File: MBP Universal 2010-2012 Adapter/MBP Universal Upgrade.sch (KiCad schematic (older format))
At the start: 3 parts, among them J1 501745-0301, J3401 500913-0302, P1 AdapterPCIEContacts

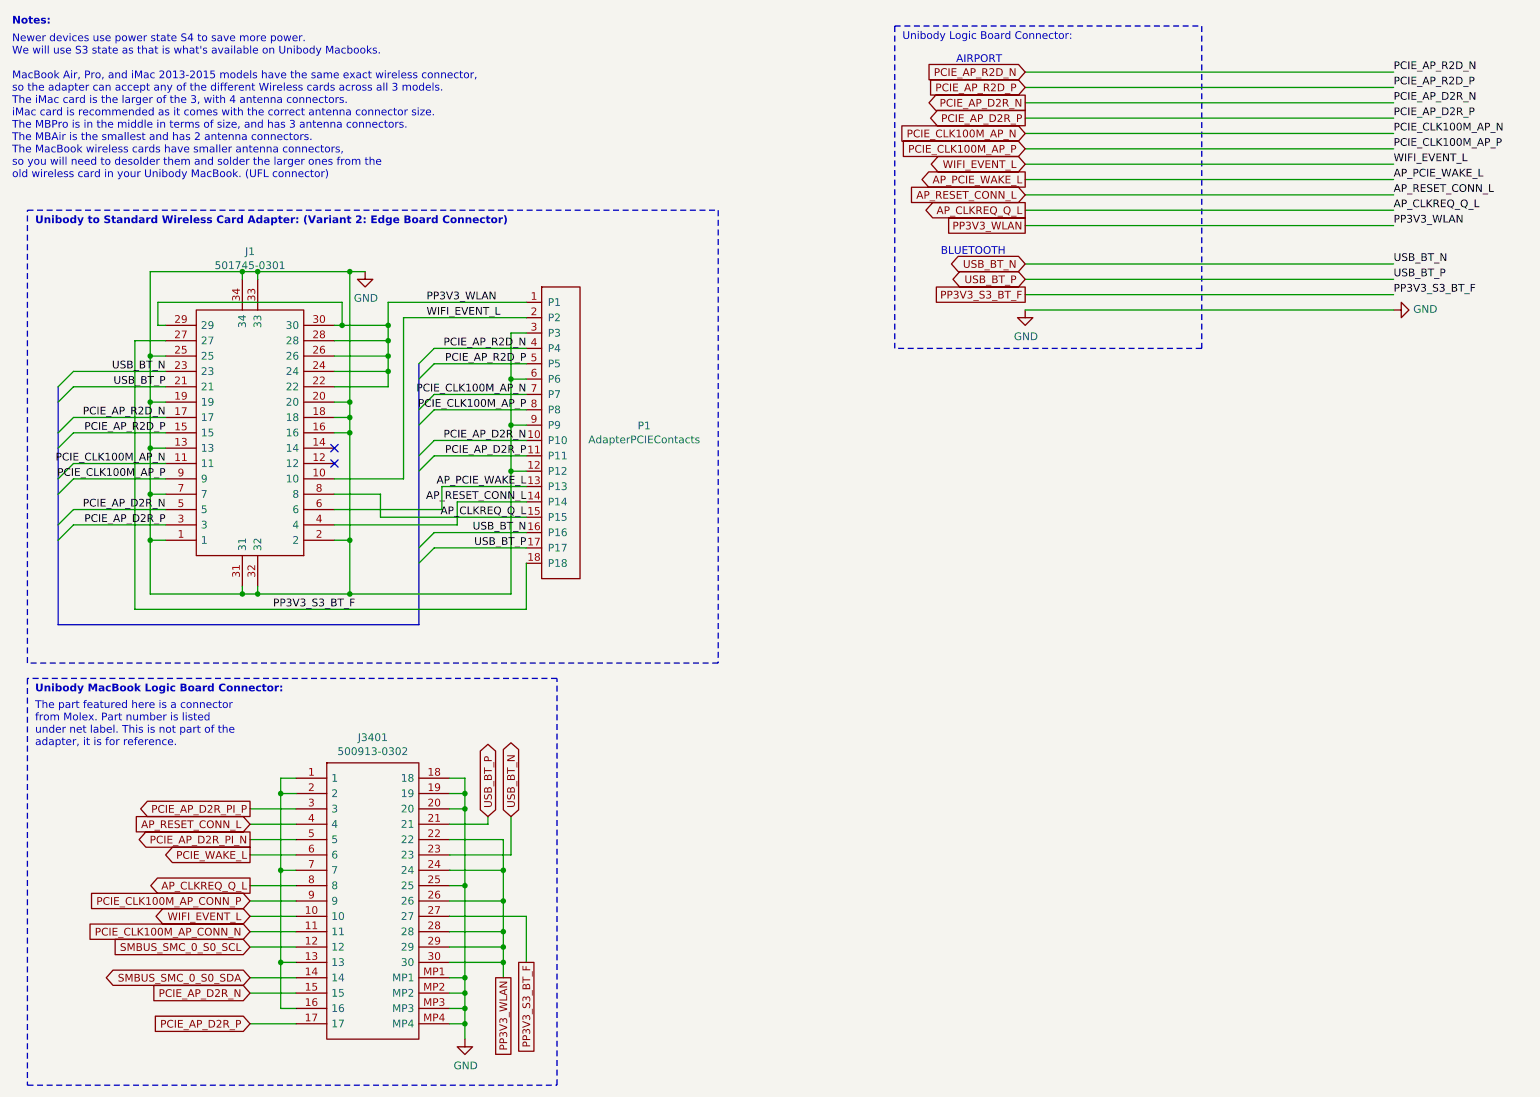
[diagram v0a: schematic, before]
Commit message: Release prototype for Universal part ready.
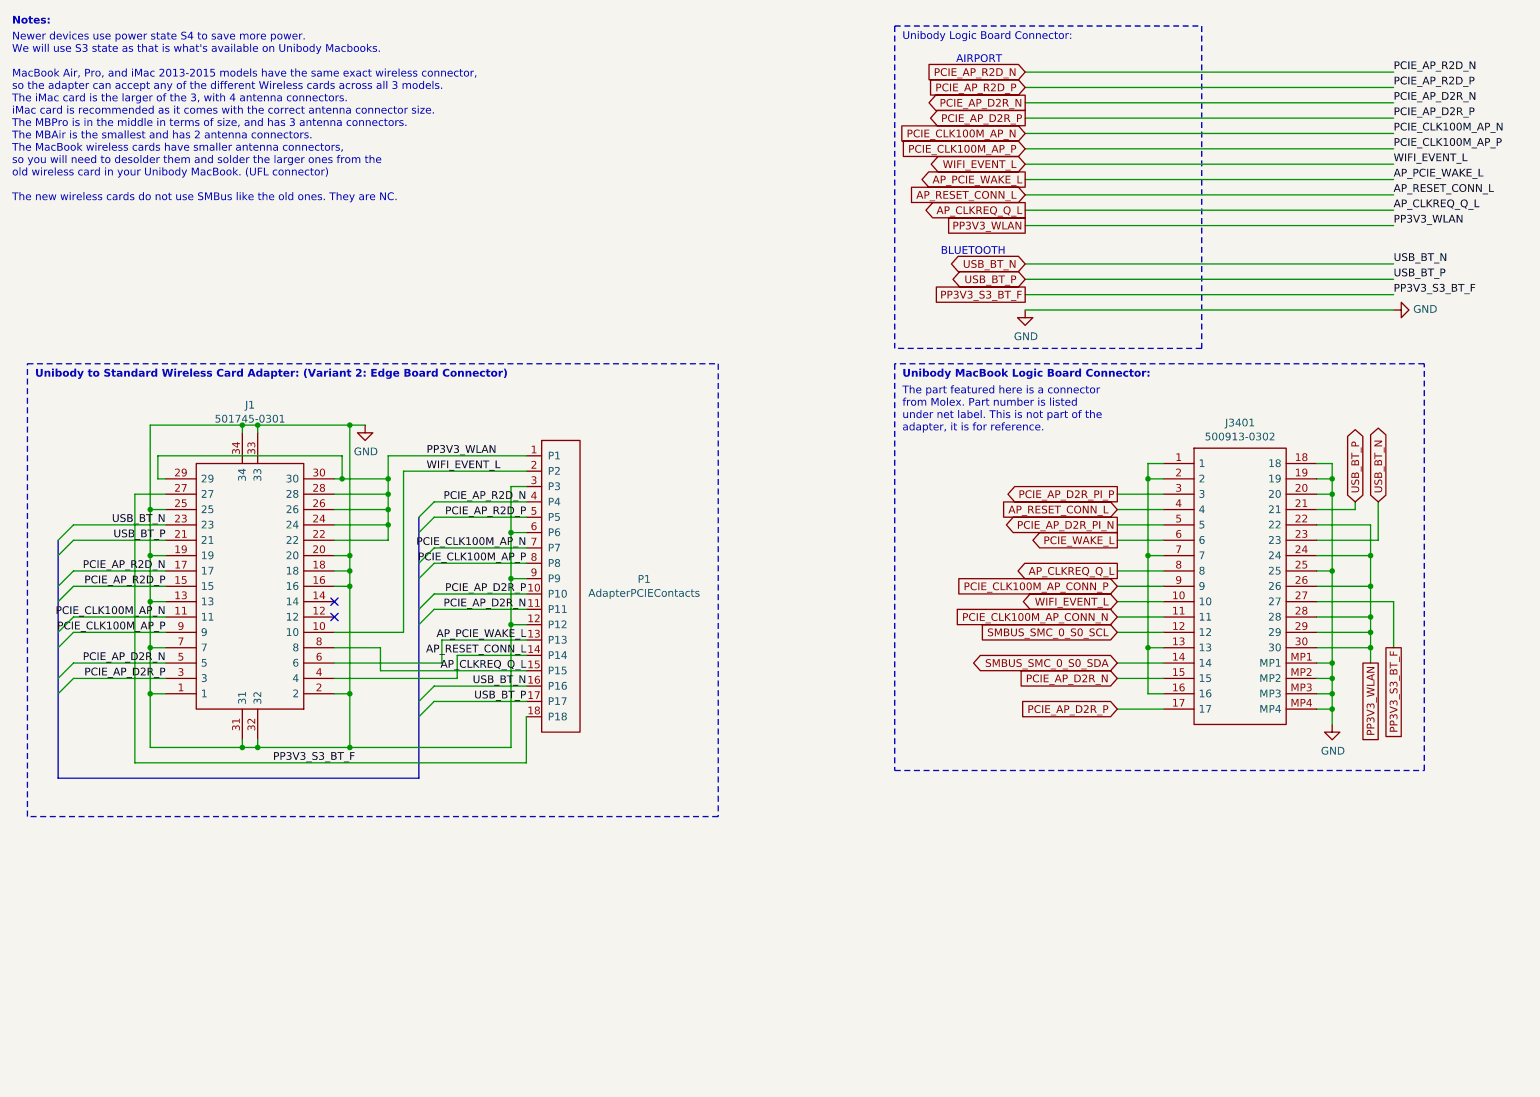
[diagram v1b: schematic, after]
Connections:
- net PCIE_AP_D2R_N: now also P1.11 (P11); no longer P1.10 (P10)
- net PCIE_AP_D2R_P: now also P1.10 (P10); no longer P1.11 (P11)
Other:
- moved on the sheet: J1, J3401, P1

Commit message: Added pre-release fabrication files
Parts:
- J1: value 501745-0301 -> Molex 501745-0301
- J3401: value 500913-0302 -> Molex 500913-0302
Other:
- note added: "Newer devices use power state S4 to save more power. \nWe will use S3 state as that is what's available on Unibody Macbooks.\n\nMacBook Air, Pro, and iMac 2013-2015 models have the same exact wireless connector, \nso the adapter can accept any of the different Wireless cards across all 3 models.\nThe iMac card is the larger of the 3, with 4 antenna connectors.\nThe MBPro is in the middle in terms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"
- note added: "Unibody to Standard Wireless Card Adapter: (Variant 1: Edge Board Connector)"
- note removed: "AIRPORT"
- note removed: "BLUETOOTH"
- note removed: "Newer devices use power state S4 to save more power. \nWe will use S3 state as that is what's available on Unibody Macbooks.\n\nMacBook Air, Pro, and iMac 2013-2015 models have the same exact wireless connector, \nso the adapter can accept any of the different Wireless cards across all 3 models.\nThe iMac card is the larger of the 3, with 4 antenna connectors.\niMac card is recommended as it come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"
- note removed: "Unibody Logic Board Connector:"
- note removed: "Unibody to Standard Wireless Card Adapter: (Variant 2: Edge Board Connector)"
- moved on the sheet: J1, J3401, P1

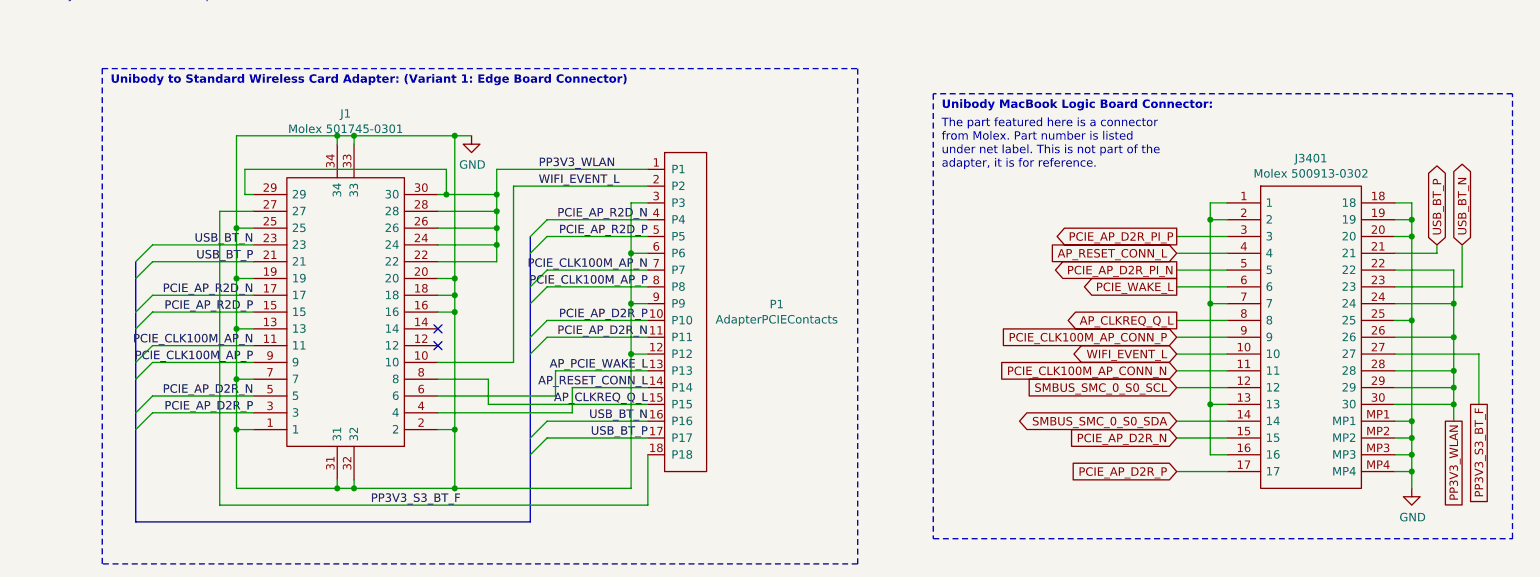
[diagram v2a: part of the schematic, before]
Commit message: Made large changes and fixes to the adapter
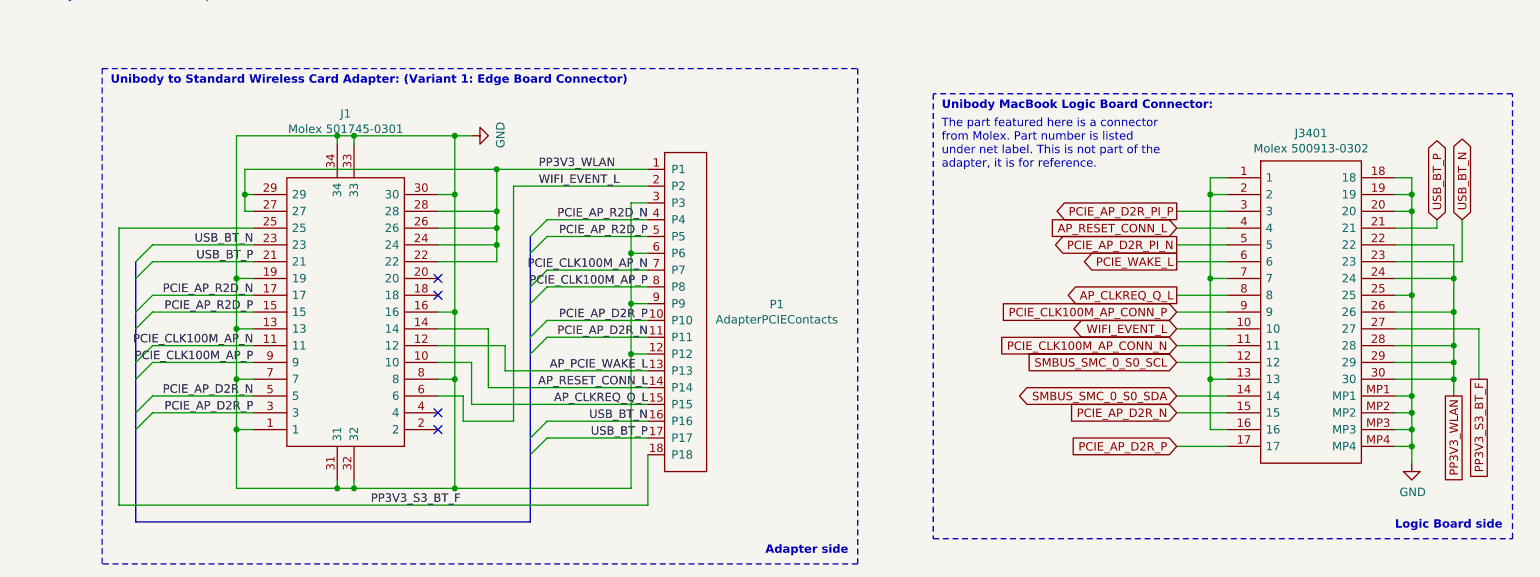
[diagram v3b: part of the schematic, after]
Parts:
- P1: footprint (none) -> MBPWirelessUpgrade:Edge Connector
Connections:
- net AP_CLKREQ_Q_L: now also J1.10; no longer J1.8
- net AP_PCIE_WAKE_L: now also J1.12; no longer J1.6
- net AP_RESET_CONN_L: now also J1.14; no longer J1.4
- net GND: now also J1.30, J1.8; no longer J1.18, J1.2, J1.20, J1.25
- net PP3V3_S3_BT_F: now also J1.25; no longer J1.27
- net PP3V3_WLAN: now also J1.27; no longer J1.30
- net WIFI_EVENT_L: now also J1.6; no longer J1.10
- no-connect marks 2 -> 4
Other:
- note added: "Adapter side"
- note added: "Logic Board side"
- moved on the sheet: J3401
